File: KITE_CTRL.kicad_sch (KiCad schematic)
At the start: 2 parts

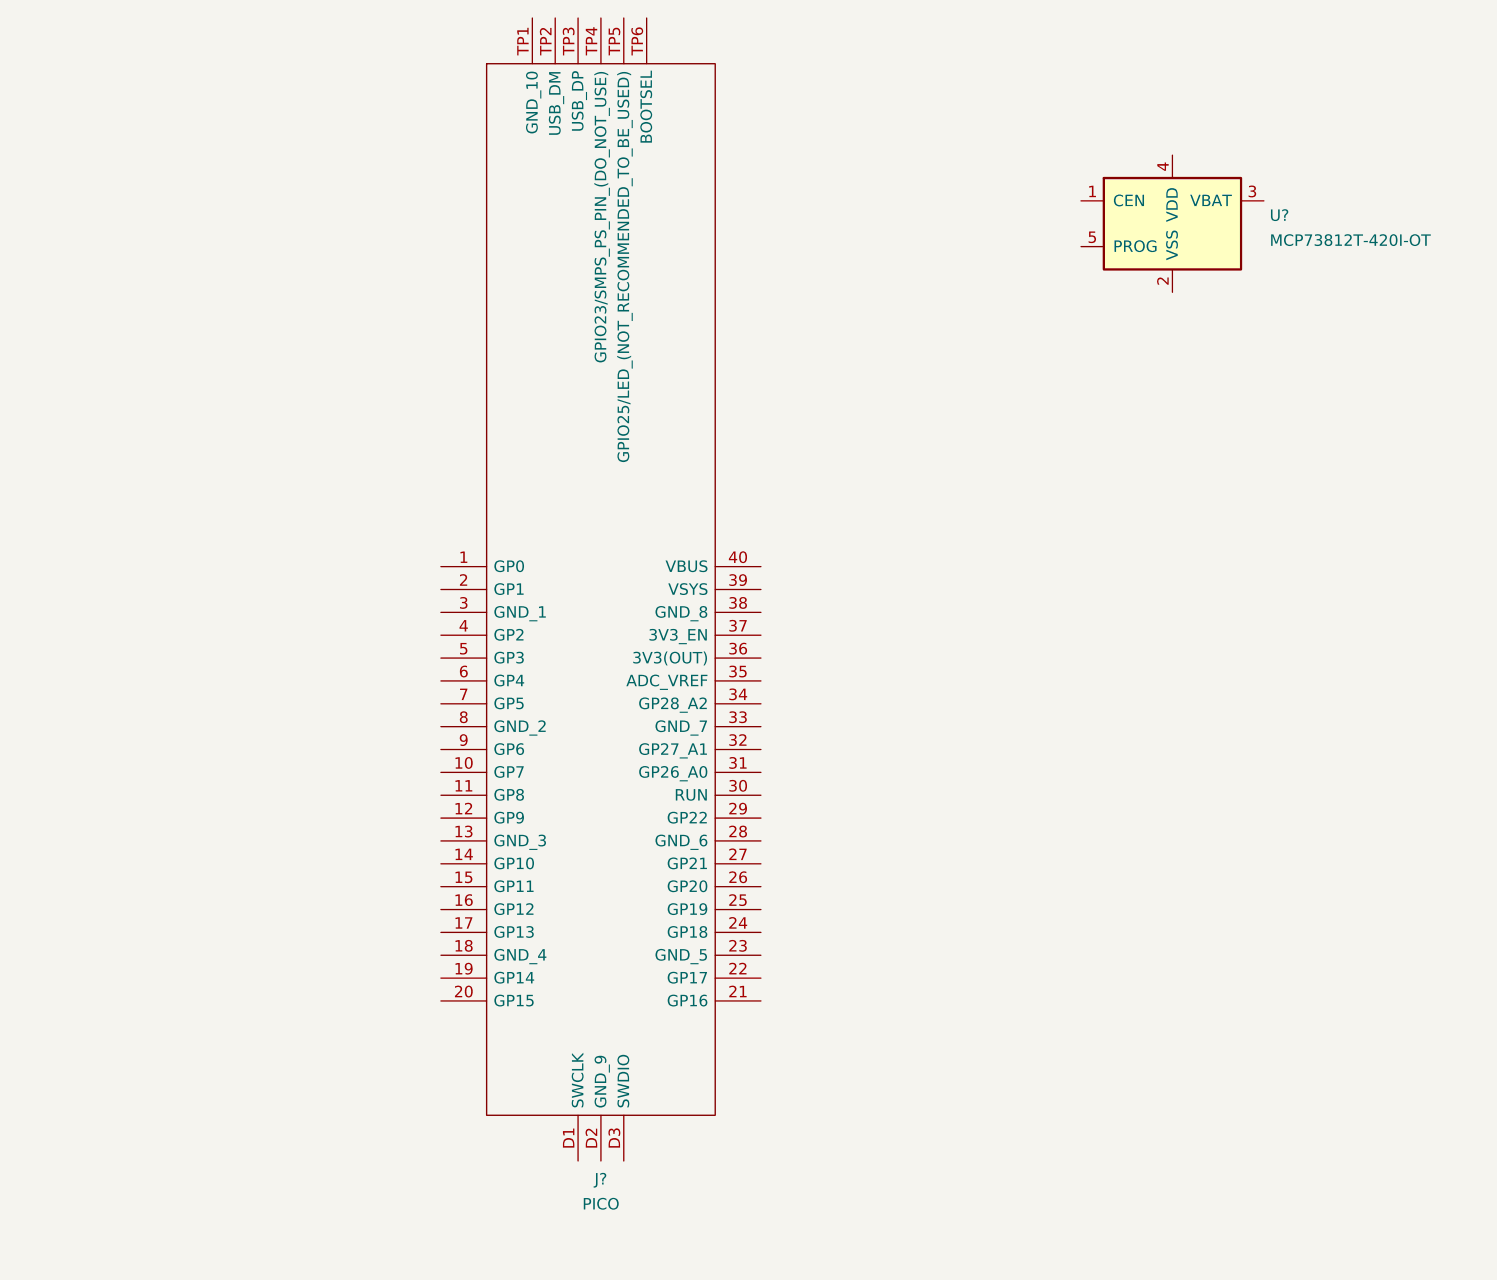
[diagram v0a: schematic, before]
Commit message: Finnished making schematic moving on to making PCB
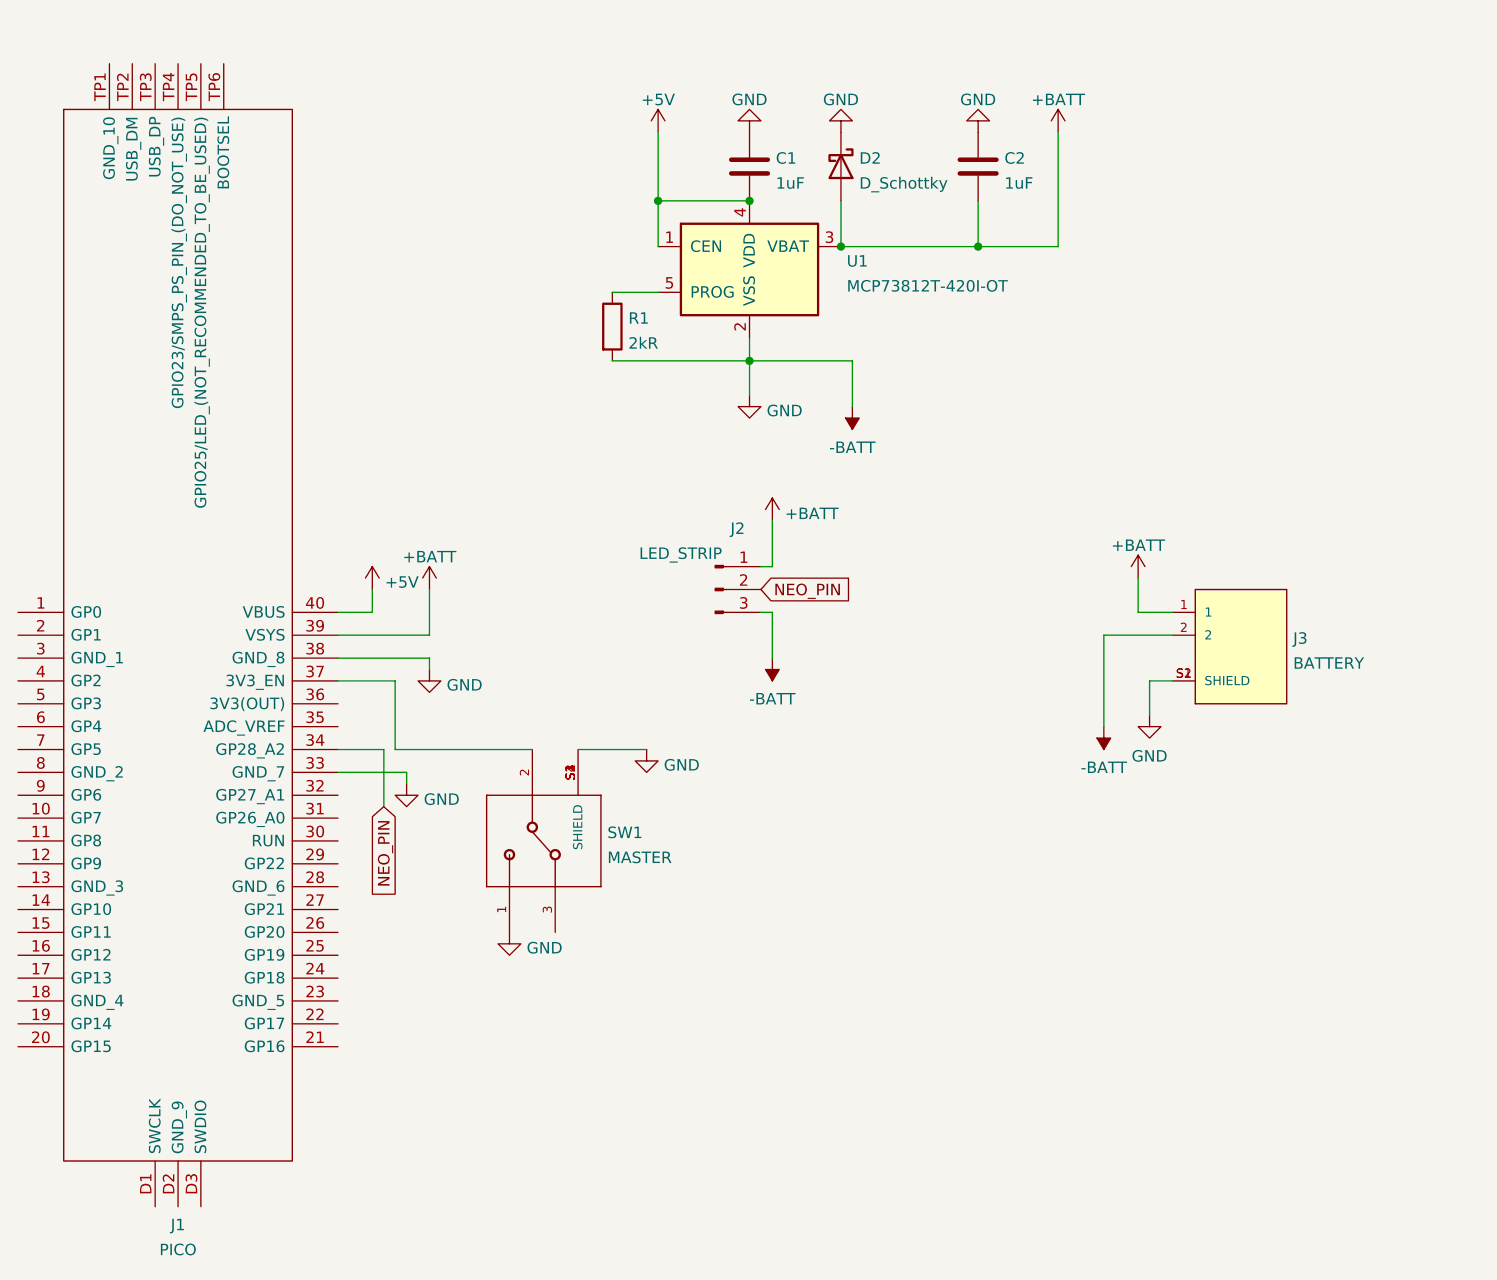
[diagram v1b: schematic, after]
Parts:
- added C1, C2: 1uF, symbol Device:C
- added D2: D_Schottky, symbol Device:D_Schottky
- added J2: LED_STRIP, symbol Connector:Conn_01x03_Male
- added J3: BATTERY, JST_S2B-PH-SM4-TB(LF)(SN), symbol S2B-PH-SM4-TB_LF__SN_:S2B-PH-SM4-TB(LF)(SN)
- added R1: 2kR, symbol Device:R
- added SW1: MASTER, SW_PCM12SMTR, symbol PCM12SMTR:PCM12SMTR
- gave numbers to parts that had none: 2
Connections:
- net -BATT: now reaches J1.33 (GND_7)
- net -BATT: now also J1.38 (GND_8), U1.2 (VSS), C1.1, C2.1, D2.1 (K), J2.3 (Pin_3), J3.2, J3.S1 (SHIELD), J3.S2 (SHIELD), R1.2, SW1.1, SW1.S1 (SHIELD), SW1.S2 (SHIELD), SW1.S3 (SHIELD), SW1.S4 (SHIELD)
- net NEO_PIN: now reaches J1.34 (GP28_A2)
- net NEO_PIN: now also J2.2 (Pin_2)
- net at J1.37 (3V3_EN): now also SW1.2
- net +BATT: now reaches J1.39 (VSYS)
- net +BATT: now also U1.3 (VBAT), C2.2, D2.2 (A), J2.1 (Pin_1), J3.1
- net +5V: now reaches J1.40 (VBUS)
- net +5V: now also U1.1 (CEN), U1.4 (VDD), C1.2
- net at U1.5 (PROG): now also R1.1
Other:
- moved on the sheet: J1, U1

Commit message: Finnished laying out the board
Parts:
- C1, C2: footprint (none) -> Capacitor_SMD:C_0402_1005Metric
- D2: footprint (none) -> Diode_SMD:D_0402_1005Metric
- J1: footprint PICO -> KiCad:PICO
- J2: footprint (none) -> Connector_PinSocket_2.54mm:PinSocket_1x03_P2.54mm_Vertical
- J3: footprint JST_S2B-PH-SM4-TB(LF)(SN) -> S2B-PH-SM4-TB_LF__SN_:JST_S2B-PH-SM4-TB(LF)(SN)
- R1: footprint (none) -> Resistor_SMD:R_0402_1005Metric
- SW1: footprint SW_PCM12SMTR -> PCM12SMTR:SW_PCM12SMTR
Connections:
- net +BATT: no longer J1.39 (VSYS)
- net -BATT: no longer D2.1 (K)
- new net: D2.1 (K), J1.39 (VSYS)
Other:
- moved on the sheet: D2
